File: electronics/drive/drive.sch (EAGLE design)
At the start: 11 parts, among them IC1 MEGA8-AI, IC2 MAX1483ESA, J1 AVR_SPI_PRG_6NS

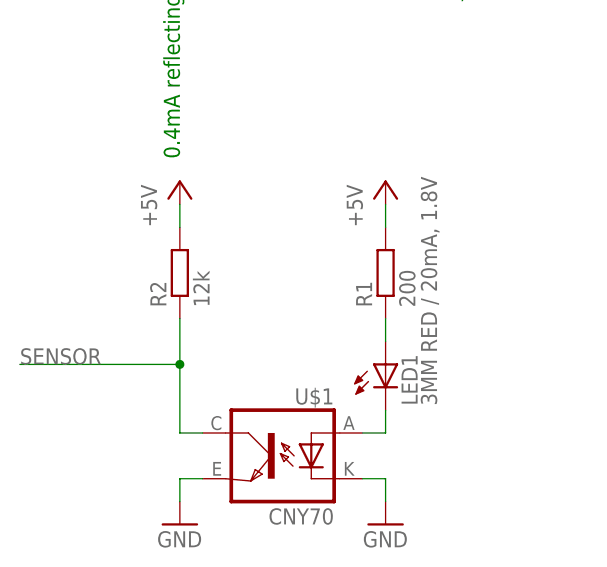
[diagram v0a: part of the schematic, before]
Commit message: Updated value of the sensor resistor on a drive board.
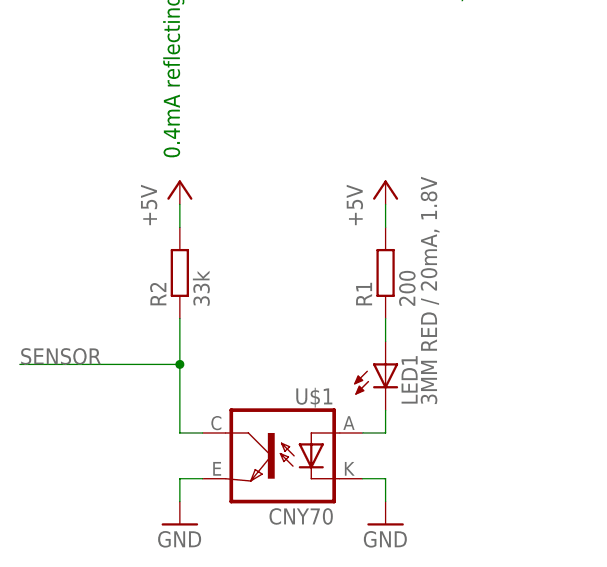
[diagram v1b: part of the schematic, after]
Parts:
- R2: value 12k -> 33k
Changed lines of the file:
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@@
 <part name="P+8" library="supply1" deviceset="+5V" device=""/>
 <part name="GND8" library="supply1" deviceset="GND" device=""/>
-<part name="R2" library="rcl" deviceset="R-EU_" device="R0805" value="12k"/>
+<part name="R2" library="rcl" deviceset="R-EU_" device="R0805" value="33k"/>
 <part name="P+6" library="supply1" deviceset="+5V" device=""/>
 <part name="R3" library="rcl" deviceset="R-EU_" device="R0805" value="1k"/>
